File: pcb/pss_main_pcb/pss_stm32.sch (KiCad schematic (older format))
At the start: 1 part

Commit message: Add stm32 schematics
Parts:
- removed U?: STM32F030F4Px, Package_SO:TSSOP-20_4.4x6.5mm_P0.65mm, symbol MCU_ST_STM32F0:STM32F030F4Px
- added C? (x2): 100n, symbol Device:C
- added C?: 4.7u, symbol Device:C
- added C?: 10n, symbol Device:C
- added C?: 1u, symbol Device:C
- added D? (x3): LED, symbol Device:LED
- added JP?: Jumper_NC_Dual, symbol Device:Jumper_NC_Dual
- added R? (x7): 1k, symbol Device:R
- added R?: 7.5, symbol Device:R
- added R? (x2): 220, symbol Device:R
- added SW?: SW_Push, symbol Switch:SW_Push
- added SW?: Soldering Iron Input, symbol Device:Rotary_Encoder_Switch
- added SW?: Hot Air Gun Input, symbol Device:Rotary_Encoder_Switch
- added U?: STM32F030K6Tx, Package_QFP:LQFP-32_7x7mm_P0.8mm, symbol MCU_ST_STM32F0:STM32F030K6Tx
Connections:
- net labels added: +3.3V, Enable_5V, Enabnle_5V, Fan_PWM, Heat_PWM, HotA_Enc_A, HotA_Enc_B, HotA_Switch, Hot_Air_Reed, Hot_Air_Themp_ADC, Iron_Themp_ADC, STM_BOOT, STM_RST, STM_SWCLK, STM_SWDIO, STM_UART_RX, STM_UART_TX, Sold_Enc_A, Sold_Enc_B, Sold_PWM, Sold_Switch
- wire segments 1 -> 94
- no-connect marks 0 -> 8
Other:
- note added: "Encoders Inputs"
- note added: "VDDA\n"
- note added: "VDD\n"

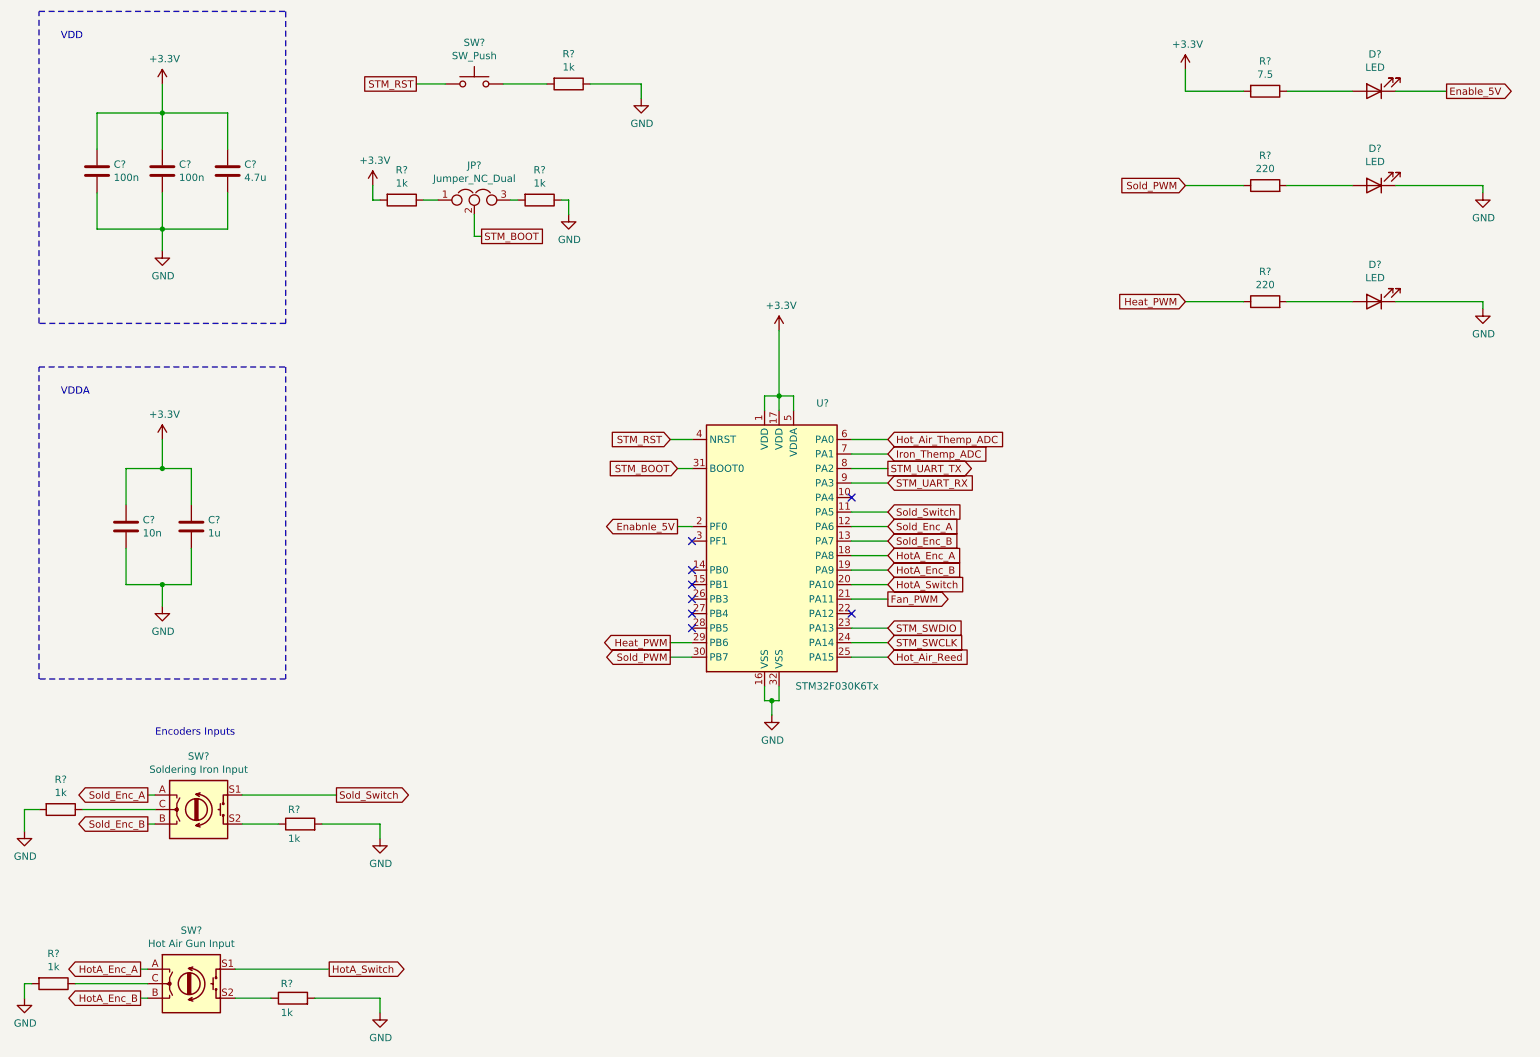
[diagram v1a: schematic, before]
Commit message: Add ESP32 to display and STM32 connections
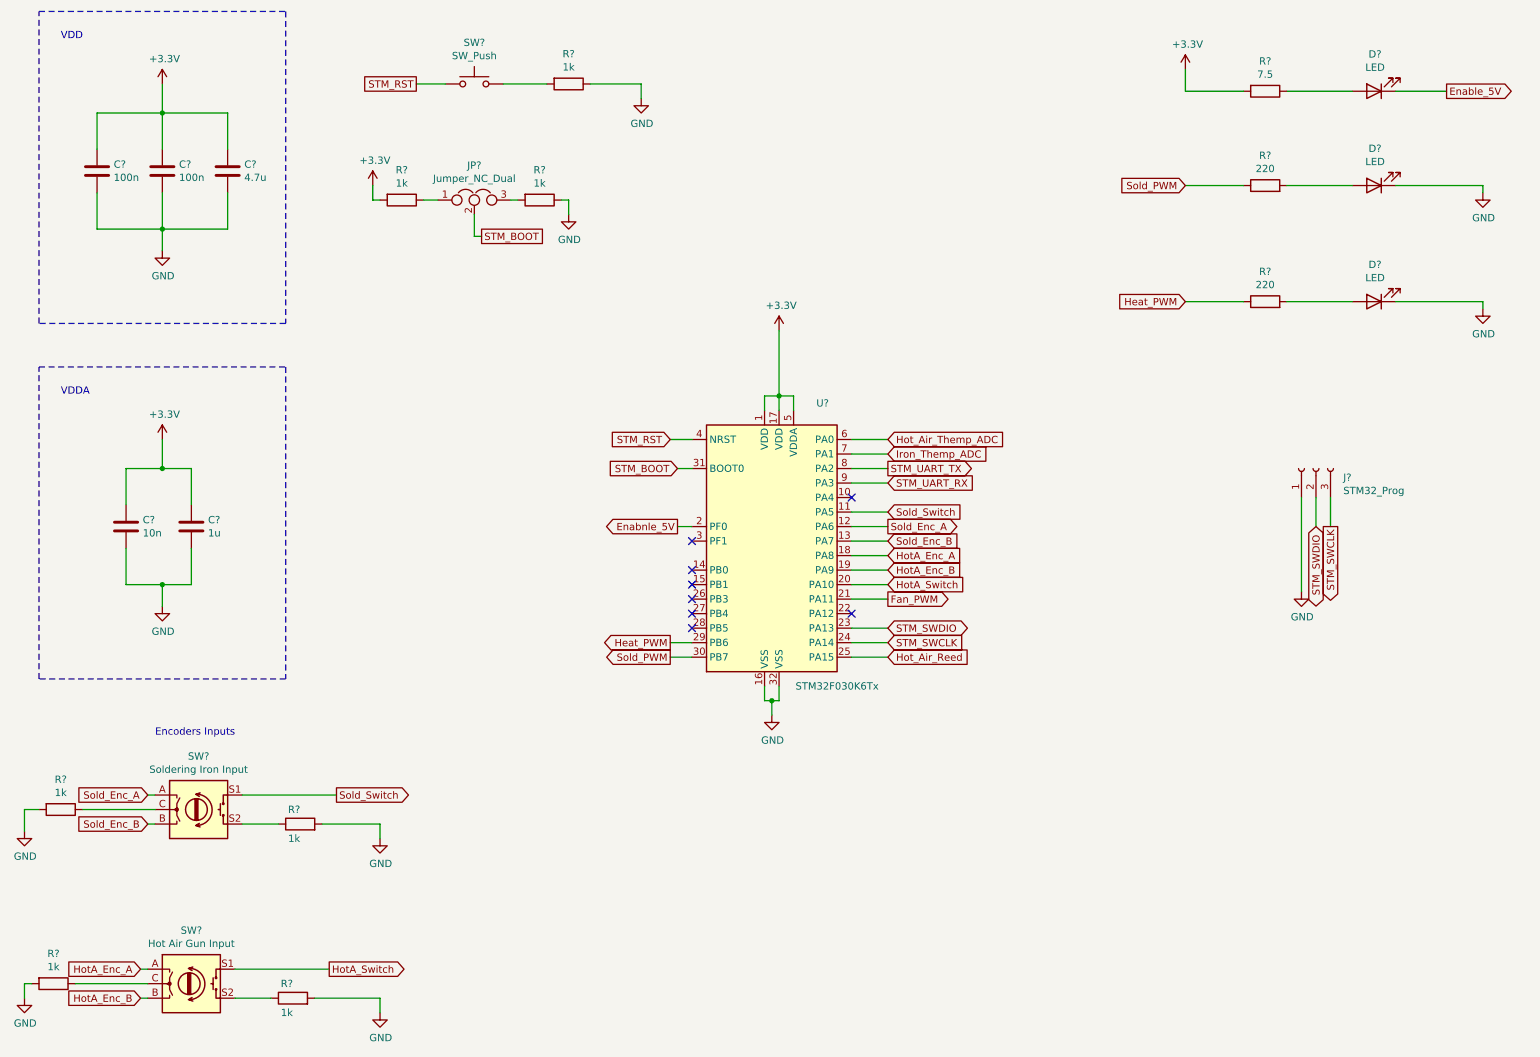
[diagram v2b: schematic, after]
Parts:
- added J?: STM32_Prog, symbol Connector:Conn_01x03_Female
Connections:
- net GND: now also J?.1 (Pin_1)
- net STM_SWCLK: now also J?.3 (Pin_3)
- net STM_SWDIO: now also J?.2 (Pin_2)
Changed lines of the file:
@@
 	0    -1   -1   0
 $EndComp
-Text GLabel 1450 6000 0    50   Output ~ 0
+Text GLabel 1450 6000 0    50   Input ~ 0
 Sold_Enc_A
-Text GLabel 1450 6200 0    50   Output ~ 0
+Text GLabel 1450 6200 0    50   Input ~ 0
 Sold_Enc_B
 Wire Wire Line
@@
 	0    -1   -1   0
 $EndComp
-Text GLabel 1400 7200 0    50   Output ~ 0
+Text GLabel 1400 7200 0    50   Input ~ 0
 HotA_Enc_A
-Text GLabel 1400 7400 0    50   Output ~ 0
+Text GLabel 1400 7400 0    50   Input ~ 0
 HotA_Enc_B
 Wire Wire Line
@@
 	6300 4050 6550 4050
 NoConn ~ 6300 3950
-Text GLabel 6550 4150 2    50   Input ~ 0
+Text GLabel 6550 4150 2    50   Output ~ 0
 Sold_Enc_A
 Text GLabel 6550 4250 2    50   Input ~ 0
@@
 Text GLabel 6550 4950 2    50   Input ~ 0
 STM_SWCLK
-Text GLabel 6550 4850 2    50   Input ~ 0
+Text GLabel 6550 4850 2    50   BiDi ~ 0
 STM_SWDIO
 Wire Wire Line
@@
 Wire Wire Line
 	9300 2600 9750 2600
+$Comp
+L Connector:Conn_01x03_Female J?
+U 1 1 5EC66EF4
+P 9500 3750
+F 0 "J?" V 9438 3562 50  0000 R CNN
+F 1 "STM32_Prog" V 9347 3562 50  0000 R CNN
+F 2 "" H 9500 3750 50  0001 C CNN
+F 3 "~" H 9500 3750 50  0001 C CNN
+	1    9500 3750
+	0    -1   -1   0
+$EndComp
+Text GLabel 9500 4150 3    50   BiDi ~ 0
+STM_SWDIO
+Wire Wire Line
+	9500 4150 9500 3950
+Text GLabel 9600 4150 3    50   Output ~ 0
+STM_SWCLK
+Wire Wire Line
+	9600 4150 9600 3950
+$Comp
+L power:GND #PWR?
+U 1 1 5EC6DA9A
+P 9400 4600
+F 0 "#PWR?" H 9400 4350 50  0001 C CNN
+F 1 "GND" H 9405 4427 50  0000 C CNN
+F 2 "" H 9400 4600 50  0001 C CNN
+F 3 "" H 9400 4600 50  0001 C CNN
+	1    9400 4600
+	1    0    0    -1
+$EndComp
+Wire Wire Line
+	9400 3950 9400 4600
 $EndSCHEMATC

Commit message: Fix schematics
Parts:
- gave numbers to parts that had none: 24
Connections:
- net Enabnle_5V is gone; now on net Enable_5V: U5.2 (PF0)
- net Heat_PWM renamed Heater_PWM

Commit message: Add some more footprints
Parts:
- J5: footprint (none) -> Connector_PinHeader_2.54mm:PinHeader_1x03_P2.54mm_Vertical
- JP1: footprint (none) -> Jumper:SolderJumper-3_P1.3mm_Open_Pad1.0x1.5mm
- SW1, SW2: footprint (none) -> Rotary_Encoder:RotaryEncoder_Alps_EC11E-Switch_Vertical_H20mm
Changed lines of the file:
@@
 F 0 "SW2" H 1800 6467 50  0000 C CNN
 F 1 "Soldering Iron Input" H 1800 6376 50  0000 C CNN
-F 2 "" H 1650 6260 50  0001 C CNN
+F 2 "Rotary_Encoder:RotaryEncoder_Alps_EC11E-Switch_Vertical_H20mm" H 1650 6260 50  0001 C CNN
 F 3 "~" H 1800 6360 50  0001 C CNN
 	1    1800 6100
@@
 F 0 "JP1" H 3700 2139 50  0000 C CNN
 F 1 "Jumper_NC_Dual" H 3700 2048 50  0000 C CNN
-F 2 "" H 3700 1900 50  0001 C CNN
+F 2 "Jumper:SolderJumper-3_P1.3mm_Open_Pad1.0x1.5mm" H 3700 1900 50  0001 C CNN
 F 3 "~" H 3700 1900 50  0001 C CNN
 	1    3700 1900
@@
 F 0 "SW1" H 1750 7667 50  0000 C CNN
 F 1 "Hot Air Gun Input" H 1750 7576 50  0000 C CNN
-F 2 "" H 1600 7460 50  0001 C CNN
+F 2 "Rotary_Encoder:RotaryEncoder_Alps_EC11E-Switch_Vertical_H20mm" H 1600 7460 50  0001 C CNN
 F 3 "~" H 1750 7560 50  0001 C CNN
 	1    1750 7300
@@
 F 0 "J5" V 9438 3562 50  0000 R CNN
 F 1 "STM32_Prog" V 9347 3562 50  0000 R CNN
-F 2 "" H 9500 3750 50  0001 C CNN
+F 2 "Connector_PinHeader_2.54mm:PinHeader_1x03_P2.54mm_Vertical" H 9500 3750 50  0001 C CNN
 F 3 "~" H 9500 3750 50  0001 C CNN
 	1    9500 3750

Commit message: Add footprints
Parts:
- C15, C16, C17, C18, C19: footprint (none) -> Capacitor_SMD:C_1206_3216Metric_Pad1.42x1.75mm_HandSolder
- D6, D7, D8: footprint (none) -> LED_THT:LED_D5.0mm
- R21, R22, R23, R24, R25, R26, R27, R28, R29, R30: footprint (none) -> Resistor_SMD:R_1206_3216Metric_Pad1.42x1.75mm_HandSolder
- SW3: footprint (none) -> Button_Switch_SMD:SW_SPST_B3S-1000
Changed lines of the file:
@@
 F 0 "C15" H 1215 1746 50  0000 L CNN
 F 1 "100n" H 1215 1655 50  0000 L CNN
-F 2 "" H 1138 1550 50  0001 C CNN
+F 2 "Capacitor_SMD:C_1206_3216Metric_Pad1.42x1.75mm_HandSolder" H 1138 1550 50  0001 C CNN
 F 3 "~" H 1100 1700 50  0001 C CNN
 	1    1100 1700
@@
 F 0 "C19" H 2115 1746 50  0000 L CNN
 F 1 "4.7u" H 2115 1655 50  0000 L CNN
-F 2 "" H 2038 1550 50  0001 C CNN
+F 2 "Capacitor_SMD:C_1206_3216Metric_Pad1.42x1.75mm_HandSolder" H 2038 1550 50  0001 C CNN
 F 3 "~" H 2000 1700 50  0001 C CNN
 	1    2000 1700
@@
 F 0 "C17" H 1665 1746 50  0000 L CNN
 F 1 "100n" H 1665 1655 50  0000 L CNN
-F 2 "" H 1588 1550 50  0001 C CNN
+F 2 "Capacitor_SMD:C_1206_3216Metric_Pad1.42x1.75mm_HandSolder" H 1588 1550 50  0001 C CNN
 F 3 "~" H 1550 1700 50  0001 C CNN
 	1    1550 1700
@@
 F 0 "C16" H 1415 4196 50  0000 L CNN
 F 1 "10n" H 1415 4105 50  0000 L CNN
-F 2 "" H 1338 4000 50  0001 C CNN
+F 2 "Capacitor_SMD:C_1206_3216Metric_Pad1.42x1.75mm_HandSolder" H 1338 4000 50  0001 C CNN
 F 3 "~" H 1300 4150 50  0001 C CNN
 	1    1300 4150
@@
 F 0 "C18" H 1865 4196 50  0000 L CNN
 F 1 "1u" H 1865 4105 50  0000 L CNN
-F 2 "" H 1788 4000 50  0001 C CNN
+F 2 "Capacitor_SMD:C_1206_3216Metric_Pad1.42x1.75mm_HandSolder" H 1788 4000 50  0001 C CNN
 F 3 "~" H 1750 4150 50  0001 C CNN
 	1    1750 4150
@@
 F 0 "SW3" H 3700 1385 50  0000 C CNN
 F 1 "SW_Push" H 3700 1294 50  0000 C CNN
-F 2 "" H 3700 1300 50  0001 C CNN
+F 2 "Button_Switch_SMD:SW_SPST_B3S-1000" H 3700 1300 50  0001 C CNN
 F 3 "~" H 3700 1300 50  0001 C CNN
 	1    3700 1100
@@
 F 0 "R24" V 2600 6200 50  0000 L CNN
 F 1 "1k" V 2400 6200 50  0000 L CNN
-F 2 "" V 2430 6200 50  0001 C CNN
+F 2 "Resistor_SMD:R_1206_3216Metric_Pad1.42x1.75mm_HandSolder" V 2430 6200 50  0001 C CNN
 F 3 "~" H 2500 6200 50  0001 C CNN
 	1    2500 6200
@@
 F 0 "R27" V 4143 1100 50  0000 C CNN
 F 1 "1k" V 4234 1100 50  0000 C CNN
-F 2 "" V 4280 1100 50  0001 C CNN
+F 2 "Resistor_SMD:R_1206_3216Metric_Pad1.42x1.75mm_HandSolder" V 4280 1100 50  0001 C CNN
 F 3 "~" H 4350 1100 50  0001 C CNN
 	1    4350 1100
@@
 F 0 "R26" V 3943 1900 50  0000 C CNN
 F 1 "1k" V 4034 1900 50  0000 C CNN
-F 2 "" V 4080 1900 50  0001 C CNN
+F 2 "Resistor_SMD:R_1206_3216Metric_Pad1.42x1.75mm_HandSolder" V 4080 1900 50  0001 C CNN
 F 3 "~" H 4150 1900 50  0001 C CNN
 	1    4150 1900
@@
 F 0 "R25" V 2993 1900 50  0000 C CNN
 F 1 "1k" V 3084 1900 50  0000 C CNN
-F 2 "" V 3130 1900 50  0001 C CNN
+F 2 "Resistor_SMD:R_1206_3216Metric_Pad1.42x1.75mm_HandSolder" V 3130 1900 50  0001 C CNN
 F 3 "~" H 3200 1900 50  0001 C CNN
 	1    3200 1900
@@
 F 0 "R23" V 2550 7400 50  0000 L CNN
 F 1 "1k" V 2350 7400 50  0000 L CNN
-F 2 "" V 2380 7400 50  0001 C CNN
+F 2 "Resistor_SMD:R_1206_3216Metric_Pad1.42x1.75mm_HandSolder" V 2380 7400 50  0001 C CNN
 F 3 "~" H 2450 7400 50  0001 C CNN
 	1    2450 7400
@@
 F 0 "R22" V 643 6100 50  0000 C CNN
 F 1 "1k" V 734 6100 50  0000 C CNN
-F 2 "" V 780 6100 50  0001 C CNN
+F 2 "Resistor_SMD:R_1206_3216Metric_Pad1.42x1.75mm_HandSolder" V 780 6100 50  0001 C CNN
 F 3 "~" H 850 6100 50  0001 C CNN
 	1    850  6100
@@
 F 0 "R21" V 593 7300 50  0000 C CNN
 F 1 "1k" V 684 7300 50  0000 C CNN
-F 2 "" V 730 7300 50  0001 C CNN
+F 2 "Resistor_SMD:R_1206_3216Metric_Pad1.42x1.75mm_HandSolder" V 730 7300 50  0001 C CNN
 F 3 "~" H 800 7300 50  0001 C CNN
 	1    800  7300
@@
 F 0 "D6" H 9893 895 50  0000 C CNN
 F 1 "LED" H 9893 986 50  0000 C CNN
-F 2 "" H 9900 1150 50  0001 C CNN
+F 2 "LED_THT:LED_D5.0mm" H 9900 1150 50  0001 C CNN
 F 3 "~" H 9900 1150 50  0001 C CNN
 	1    9900 1150
@@
 F 0 "R28" V 8943 1150 50  0000 C CNN
 F 1 "7.5" V 9034 1150 50  0000 C CNN
-F 2 "" V 9080 1150 50  0001 C CNN
+F 2 "Resistor_SMD:R_1206_3216Metric_Pad1.42x1.75mm_HandSolder" V 9080 1150 50  0001 C CNN
 F 3 "~" H 9150 1150 50  0001 C CNN
 	1    9150 1150
@@
 F 0 "D7" H 9893 1545 50  0000 C CNN
 F 1 "LED" H 9893 1636 50  0000 C CNN
-F 2 "" H 9900 1800 50  0001 C CNN
+F 2 "LED_THT:LED_D5.0mm" H 9900 1800 50  0001 C CNN
 F 3 "~" H 9900 1800 50  0001 C CNN
 	1    9900 1800
@@
 F 0 "R29" V 9357 1800 50  0000 C CNN
 F 1 "220" V 9266 1800 50  0000 C CNN
-F 2 "" V 9080 1800 50  0001 C CNN
+F 2 "Resistor_SMD:R_1206_3216Metric_Pad1.42x1.75mm_HandSolder" V 9080 1800 50  0001 C CNN
 F 3 "~" H 9150 1800 50  0001 C CNN
 	1    9150 1800
@@
 F 0 "D8" H 9893 2345 50  0000 C CNN
 F 1 "LED" H 9893 2436 50  0000 C CNN
-F 2 "" H 9900 2600 50  0001 C CNN
+F 2 "LED_THT:LED_D5.0mm" H 9900 2600 50  0001 C CNN
 F 3 "~" H 9900 2600 50  0001 C CNN
 	1    9900 2600
@@
 F 0 "R30" V 9357 2600 50  0000 C CNN
 F 1 "220" V 9266 2600 50  0000 C CNN
-F 2 "" V 9080 2600 50  0001 C CNN
+F 2 "Resistor_SMD:R_1206_3216Metric_Pad1.42x1.75mm_HandSolder" V 9080 2600 50  0001 C CNN
 F 3 "~" H 9150 2600 50  0001 C CNN
 	1    9150 2600
